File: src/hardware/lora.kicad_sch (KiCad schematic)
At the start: 19 parts, among them IC1 LLCC68IMLTRT, U20 TPS22916BYFPR, U21 0900FM15K0039001E, U22 BGS12WN6E6327XTSA1, Y4 NSC5359C-32M

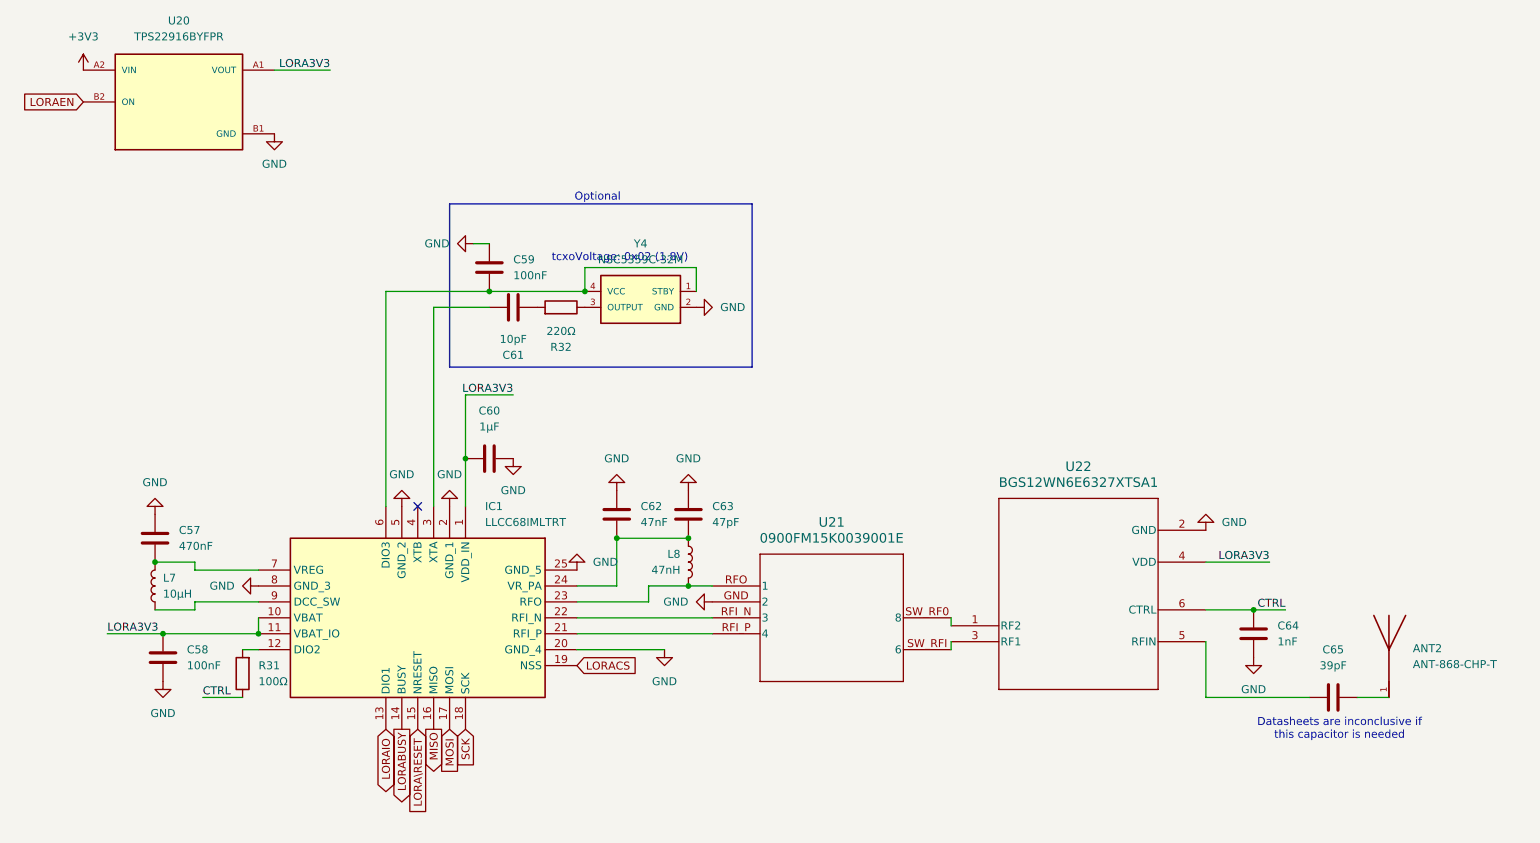
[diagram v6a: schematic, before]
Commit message: Add Light Sensor and Proximity & Gesture Sensor; Changed GPIO
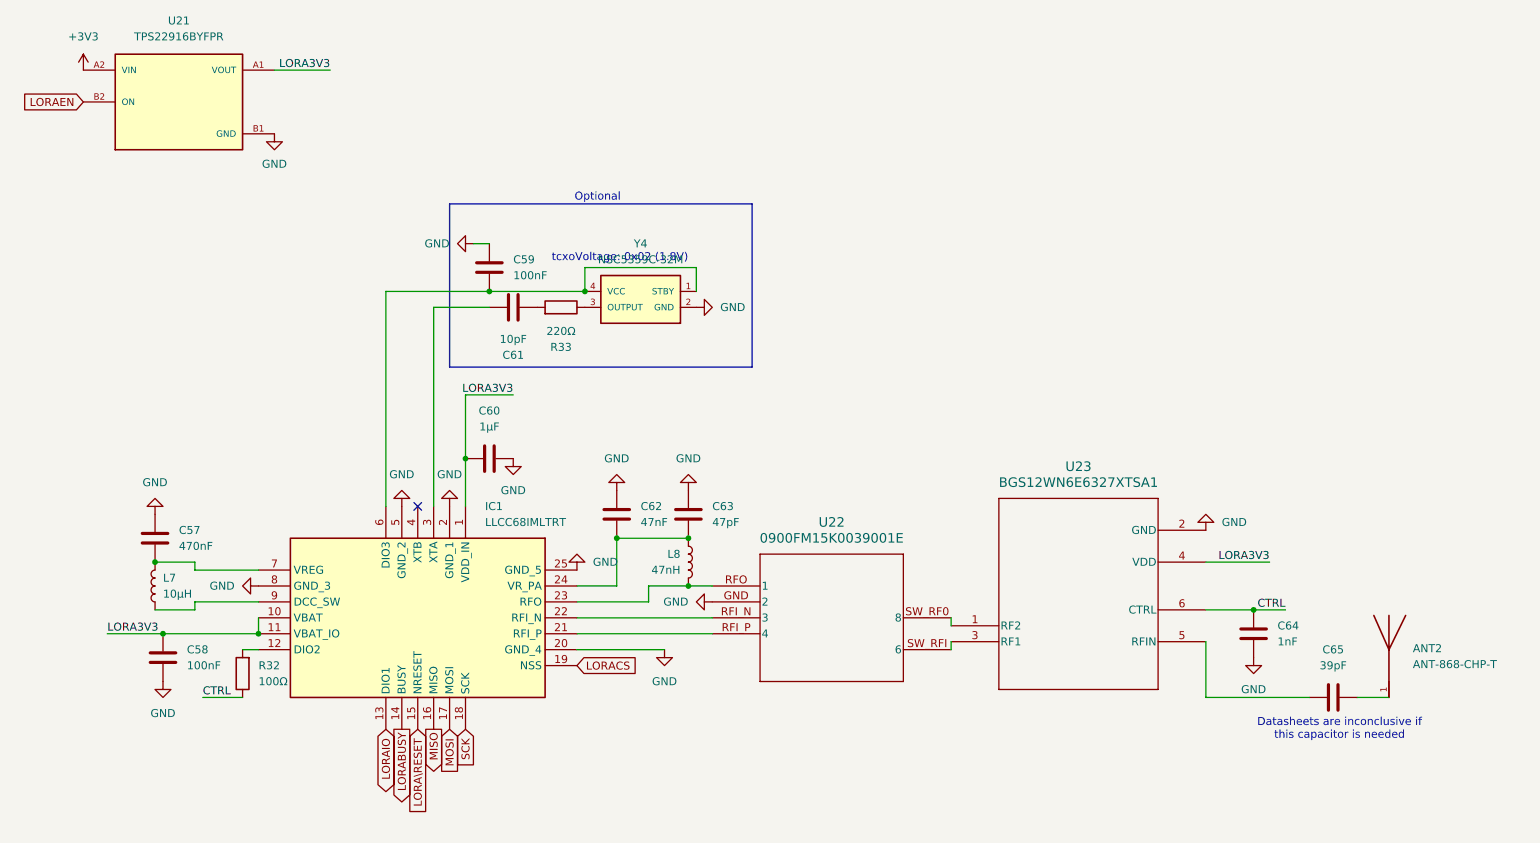
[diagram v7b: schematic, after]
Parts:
- renumbered R31 to R32, R32 to R33, U20 to U21, U21 to U22, U22 to U23
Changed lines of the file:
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@@
 		(dnp no)
 		(fields_autoplaced yes)
-		(property "Reference" "U20"
+		(property "Reference" "U21"
 			(at 54.61 22.86 0)
 			(effects
@@
 			(project "raywatch"
 				(path "/7b654ee8-2a53-4d39-8b7d-32c7bb3cb0ed/500b48f3-f083-4626-a865-624bdd615c7c"
-					(reference "U20")
+					(reference "U21")
 					(unit 1)
 				)
@@
 		(dnp no)
 		(fields_autoplaced yes)
-		(property "Reference" "R31"
+		(property "Reference" "R32"
 			(at 67.31 125.7299 0)
 			(effects
@@
 			(project "raywatch"
 				(path "/7b654ee8-2a53-4d39-8b7d-32c7bb3cb0ed/500b48f3-f083-4626-a865-624bdd615c7c"
-					(reference "R31")
+					(reference "R32")
 					(unit 1)
 				)
@@
 		(dnp no)
 		(fields_autoplaced yes)
-		(property "Reference" "U21"
+		(property "Reference" "U22"
 			(at 158.75 102.87 0)
 			(effects
@@
 			(project "raywatch"
 				(path "/7b654ee8-2a53-4d39-8b7d-32c7bb3cb0ed/500b48f3-f083-4626-a865-624bdd615c7c"
-					(reference "U21")
+					(reference "U22")
 					(unit 1)
 				)
@@
 		(dnp no)
 		(fields_autoplaced yes)
-		(property "Reference" "#PWR0330"
+		(property "Reference" "#PWR0334"
 			(at 132.08 129.54 0)
 			(effects
@@
 			(project "raywatch"
 				(path "/7b654ee8-2a53-4d39-8b7d-32c7bb3cb0ed/500b48f3-f083-4626-a865-624bdd615c7c"
-					(reference "#PWR0330")
+					(reference "#PWR0334")
 					(unit 1)
 				)
@@
 		(dnp no)
 		(fields_autoplaced yes)
-		(property "Reference" "#PWR0320"
+		(property "Reference" "#PWR0324"
 			(at 50.8 95.25 0)
 			(effects
@@
 			(project "raywatch"
 				(path "/7b654ee8-2a53-4d39-8b7d-32c7bb3cb0ed/500b48f3-f083-4626-a865-624bdd615c7c"
-					(reference "#PWR0320")
+					(reference "#PWR0324")
 					(unit 1)
 				)
@@
 		(dnp no)
 		(fields_autoplaced yes)
-		(property "Reference" "#PWR0321"
+		(property "Reference" "#PWR0325"
 			(at 52.07 134.62 0)
 			(effects
@@
 			(project "raywatch"
 				(path "/7b654ee8-2a53-4d39-8b7d-32c7bb3cb0ed/500b48f3-f083-4626-a865-624bdd615c7c"
-					(reference "#PWR0321")
+					(reference "#PWR0325")
 					(unit 1)
 				)
@@
 		(dnp no)
 		(fields_autoplaced yes)
-		(property "Reference" "#PWR0322"
+		(property "Reference" "#PWR0326"
 			(at 60.96 113.03 0)
 			(effects
@@
 			(project "raywatch"
 				(path "/7b654ee8-2a53-4d39-8b7d-32c7bb3cb0ed/500b48f3-f083-4626-a865-624bdd615c7c"
-					(reference "#PWR0322")
+					(reference "#PWR0326")
 					(unit 1)
 				)
@@
 		(dnp no)
 		(fields_autoplaced yes)
-		(property "Reference" "#PWR0323"
+		(property "Reference" "#PWR0327"
 			(at 69.85 47.244 0)
 			(effects
@@
 			(project "raywatch"
 				(path "/7b654ee8-2a53-4d39-8b7d-32c7bb3cb0ed/500b48f3-f083-4626-a865-624bdd615c7c"
-					(reference "#PWR0323")
+					(reference "#PWR0327")
 					(unit 1)
 				)
@@
 		(dnp no)
 		(fields_autoplaced yes)
-		(property "Reference" "#PWR0333"
+		(property "Reference" "#PWR0337"
 			(at 133.35 115.57 0)
 			(effects
@@
 			(project "raywatch"
 				(path "/7b654ee8-2a53-4d39-8b7d-32c7bb3cb0ed/500b48f3-f083-4626-a865-624bdd615c7c"
-					(reference "#PWR0333")
+					(reference "#PWR0337")
 					(unit 1)
 				)
@@
 		(dnp no)
 		(fields_autoplaced yes)
-		(property "Reference" "R32"
+		(property "Reference" "R33"
 			(at 115.57 74.93 90)
 			(effects
@@
 			(project "raywatch"
 				(path "/7b654ee8-2a53-4d39-8b7d-32c7bb3cb0ed/500b48f3-f083-4626-a865-624bdd615c7c"
-					(reference "R32")
+					(reference "R33")
 					(unit 1)
 				)
@@
 		(dnp no)
 		(fields_autoplaced yes)
-		(property "Reference" "#PWR0327"
+		(property "Reference" "#PWR0331"
 			(at 107.95 99.06 0)
 			(effects
@@
 			(project "raywatch"
 				(path "/7b654ee8-2a53-4d39-8b7d-32c7bb3cb0ed/500b48f3-f083-4626-a865-624bdd615c7c"
-					(reference "#PWR0327")
+					(reference "#PWR0331")
 					(unit 1)
 				)
@@
 		(dnp no)
 		(fields_autoplaced yes)
-		(property "Reference" "#PWR0334"
+		(property "Reference" "#PWR0338"
 			(at 218.44 97.79 0)
 			(effects
@@
 			(project "raywatch"
 				(path "/7b654ee8-2a53-4d39-8b7d-32c7bb3cb0ed/500b48f3-f083-4626-a865-624bdd615c7c"
-					(reference "#PWR0334")
+					(reference "#PWR0338")
 					(unit 1)
 				)
@@
 		(dnp no)
 		(fields_autoplaced yes)
-		(property "Reference" "U22"
+		(property "Reference" "U23"
 			(at 198.12 93.98 0)
 			(effects
@@
 			(project "raywatch"
 				(path "/7b654ee8-2a53-4d39-8b7d-32c7bb3cb0ed/500b48f3-f083-4626-a865-624bdd615c7c"
-					(reference "U22")
+					(reference "U23")
 					(unit 1)
 				)
@@
 		(dnp no)
 		(fields_autoplaced yes)
-		(property "Reference" "#PWR0329"
+		(property "Reference" "#PWR0333"
 			(at 124.46 91.44 0)
 			(effects
@@
 			(project "raywatch"
 				(path "/7b654ee8-2a53-4d39-8b7d-32c7bb3cb0ed/500b48f3-f083-4626-a865-624bdd615c7c"
-					(reference "#PWR0329")
+					(reference "#PWR0333")
 					(unit 1)
 				)
@@
 		(dnp no)
 		(fields_autoplaced yes)
-		(property "Reference" "#PWR0331"
+		(property "Reference" "#PWR0335"
 			(at 135.89 91.44 0)
 			(effects
@@
 			(project "raywatch"
 				(path "/7b654ee8-2a53-4d39-8b7d-32c7bb3cb0ed/500b48f3-f083-4626-a865-624bdd615c7c"
-					(reference "#PWR0331")
+					(reference "#PWR0335")
 					(unit 1)
 				)
@@
 		(dnp no)
 		(fields_autoplaced yes)
-		(property "Reference" "#PWR0325"
+		(property "Reference" "#PWR0329"
 			(at 97.79 93.98 0)
 			(effects
@@
 			(project "raywatch"
 				(path "/7b654ee8-2a53-4d39-8b7d-32c7bb3cb0ed/500b48f3-f083-4626-a865-624bdd615c7c"
-					(reference "#PWR0325")
+					(reference "#PWR0329")
 					(unit 1)
 				)
@@
 		(dnp no)
 		(fields_autoplaced yes)
-		(property "Reference" "#PWR0319"
+		(property "Reference" "#PWR0323"
 			(at 39.37 34.544 0)
 			(effects
@@
 			(project "raywatch"
 				(path "/7b654ee8-2a53-4d39-8b7d-32c7bb3cb0ed/500b48f3-f083-4626-a865-624bdd615c7c"
-					(reference "#PWR0319")
+					(reference "#PWR0323")
 					(unit 1)
 				)
@@
 		(dnp no)
 		(fields_autoplaced yes)
-		(property "Reference" "#PWR0326"
+		(property "Reference" "#PWR0330"
 			(at 95.25 58.42 0)
 			(effects
@@
 			(project "raywatch"
 				(path "/7b654ee8-2a53-4d39-8b7d-32c7bb3cb0ed/500b48f3-f083-4626-a865-624bdd615c7c"
-					(reference "#PWR0326")
+					(reference "#PWR0330")
 					(unit 1)
 				)
@@
 		(dnp no)
 		(fields_autoplaced yes)
-		(property "Reference" "#PWR0332"
+		(property "Reference" "#PWR0336"
 			(at 143.51 68.58 0)
 			(effects
@@
 			(project "raywatch"
 				(path "/7b654ee8-2a53-4d39-8b7d-32c7bb3cb0ed/500b48f3-f083-4626-a865-624bdd615c7c"
-					(reference "#PWR0332")
+					(reference "#PWR0336")
 					(unit 1)
 				)
@@
 		(dnp no)
 		(fields_autoplaced yes)
-		(property "Reference" "#PWR0324"
+		(property "Reference" "#PWR0328"
 			(at 90.17 93.98 0)
 			(effects
@@
 			(project "raywatch"
 				(path "/7b654ee8-2a53-4d39-8b7d-32c7bb3cb0ed/500b48f3-f083-4626-a865-624bdd615c7c"
-					(reference "#PWR0324")
+					(reference "#PWR0328")
 					(unit 1)
 				)
@@
 		(dnp no)
 		(fields_autoplaced yes)
-		(property "Reference" "#PWR0335"
+		(property "Reference" "#PWR0339"
 			(at 226.06 130.81 0)
 			(effects
@@
 			(project "raywatch"
 				(path "/7b654ee8-2a53-4d39-8b7d-32c7bb3cb0ed/500b48f3-f083-4626-a865-624bdd615c7c"
-					(reference "#PWR0335")
+					(reference "#PWR0339")
 					(unit 1)
 				)
@@
 		(dnp no)
 		(fields_autoplaced yes)
-		(property "Reference" "#PWR0328"
+		(property "Reference" "#PWR0332"
 			(at 118.11 104.14 0)
 			(effects
@@
 			(project "raywatch"
 				(path "/7b654ee8-2a53-4d39-8b7d-32c7bb3cb0ed/500b48f3-f083-4626-a865-624bdd615c7c"
-					(reference "#PWR0328")
-					(unit 1)
-				)
+					(reference "#PWR0332")
+					(unit 1)
+				)
